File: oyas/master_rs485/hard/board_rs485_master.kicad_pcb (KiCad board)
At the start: 2 copper layers, 132.4 x 70.8 mm, 64 parts, among them J1 POWER_12V, J2 Log, J3 POWER_OYAS_12V, J4 BUS_OYAS, J5 Leds RGB, J6 Button, J7 Adapt BUS, Q1 BPC_2N2222A, Q2 P03P4L-04, Q3 BC327, Q4 BC327, Q5 BPC_2N2222A, Q6 BPC_2N2222A, U1 RtcArduino, U2 BPC_Alim5V, U3 BPC_ESP8266-01_ESP-01, U4 BPC_Mod485, U5 LM1117DT-3.3

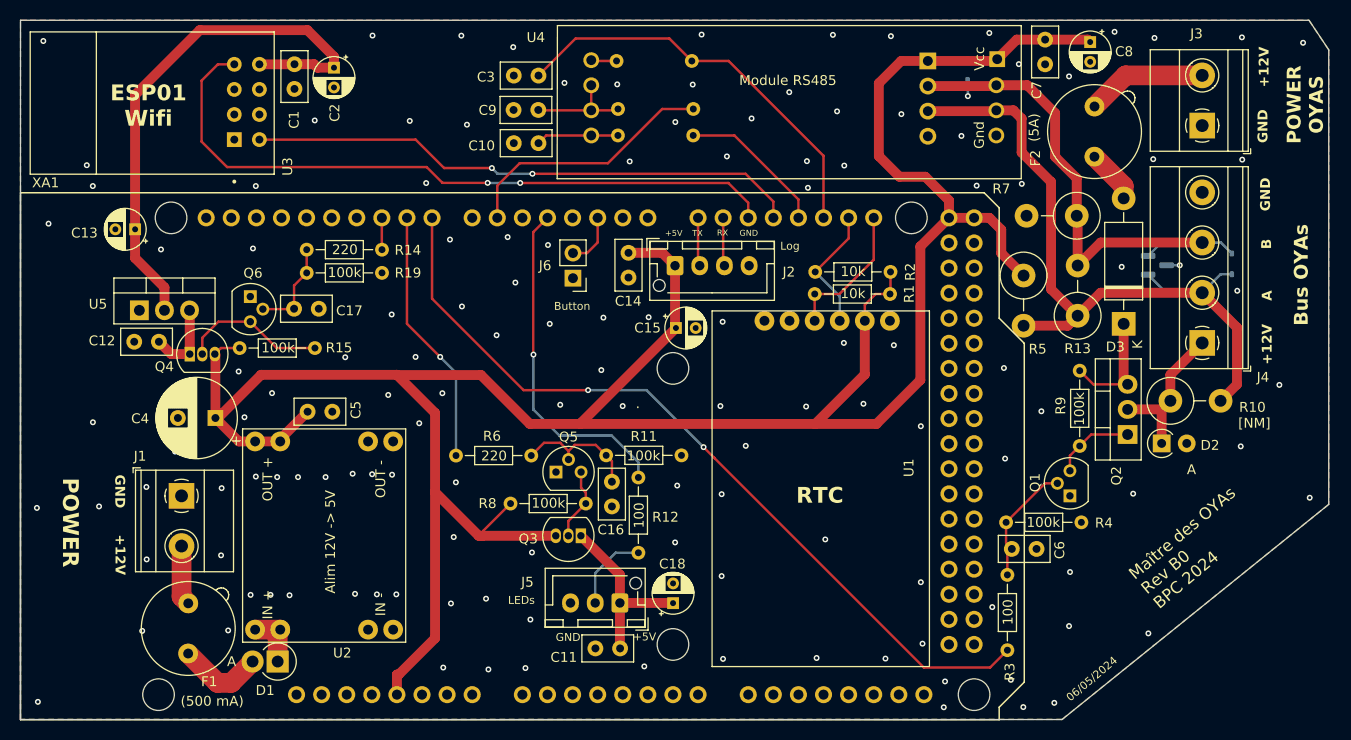
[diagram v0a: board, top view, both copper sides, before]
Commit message: MAJ correction limitation du courant de base des pnp (Pwr Wifi et LEDs)
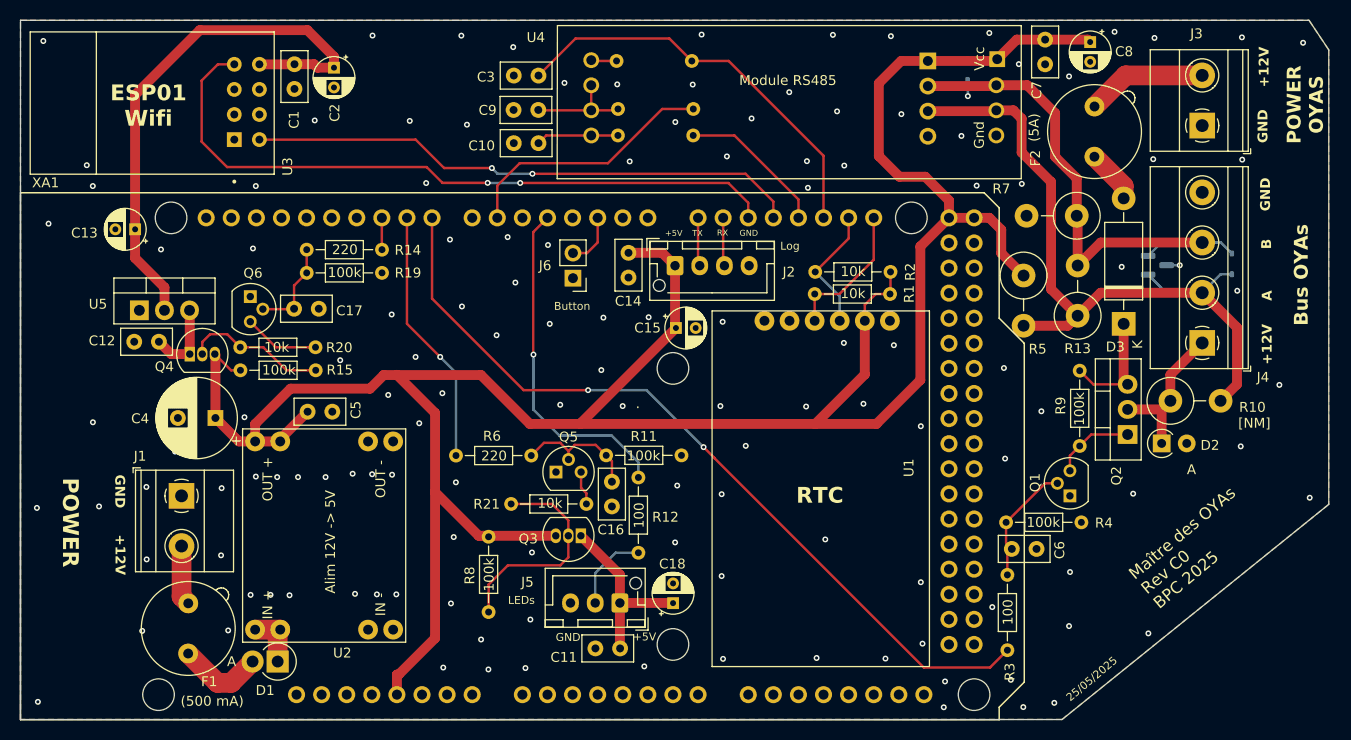
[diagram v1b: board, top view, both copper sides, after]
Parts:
- added R20: 10k, Resistor_THT:R_Axial_DIN0204_L3.6mm_D1.6mm_P7.62mm_Horizontal, F.Cu at (104.4, 82.1)
- added R21: 10k, Resistor_THT:R_Axial_DIN0204_L3.6mm_D1.6mm_P7.62mm_Horizontal, F.Cu at (131.9, 98.0)
- moved R8 4.03 mm to (122.0, 101.3), turned to -90 degrees
- moved R15 2.25 mm to (96.8, 84.4)
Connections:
- Q5 pad 3: Net-(Q3-B) -> Net-(Q5-Pad3)
- Q6 pad 3: Net-(Q4-B) -> Net-(Q6-Pad3)
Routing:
- net Net-(Q3-B): track 7.38 -> 22.2 mm
- net Net-(Q6-Pad3): track 0.00 -> 7.67 mm
- net +5V: track 270.2 -> 264.3 mm
- net Net-(Q5-Pad3): track 0.00 -> 3.45 mm
- net GND: vias 136 -> 134
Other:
- board text added: "25/05/2025"
- board text added: "Maître des OYAs Rev C0 BPC 2025"
- board text removed: "06/05/2024"
- board text removed: "Maître des OYAs Rev B0 BPC 2024"
